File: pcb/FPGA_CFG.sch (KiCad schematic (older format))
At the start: 5 parts, among them U4 iCE40-HX8K-CT256, U6 SERIAL_FLASH

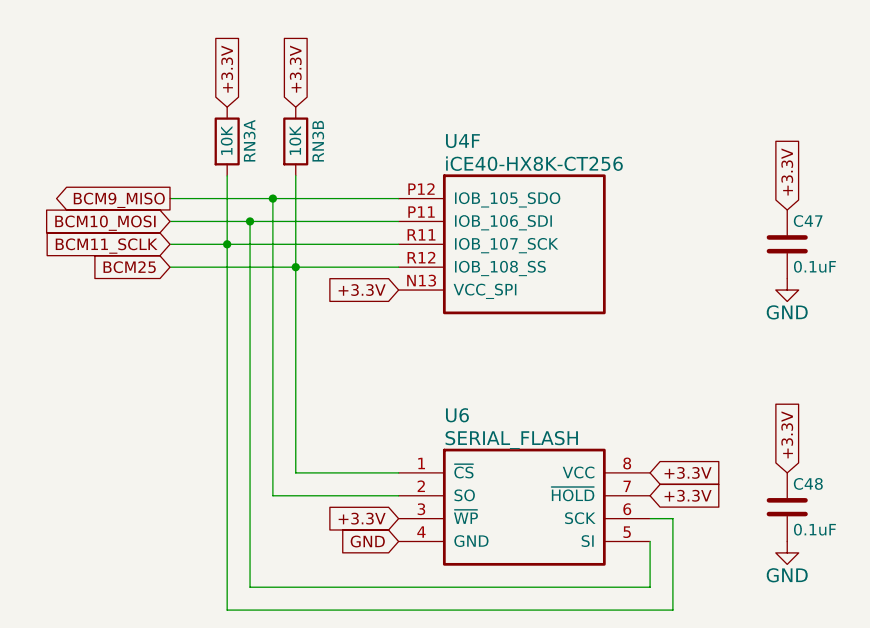
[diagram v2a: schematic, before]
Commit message: Added manufacturer part numbers to the schematic.
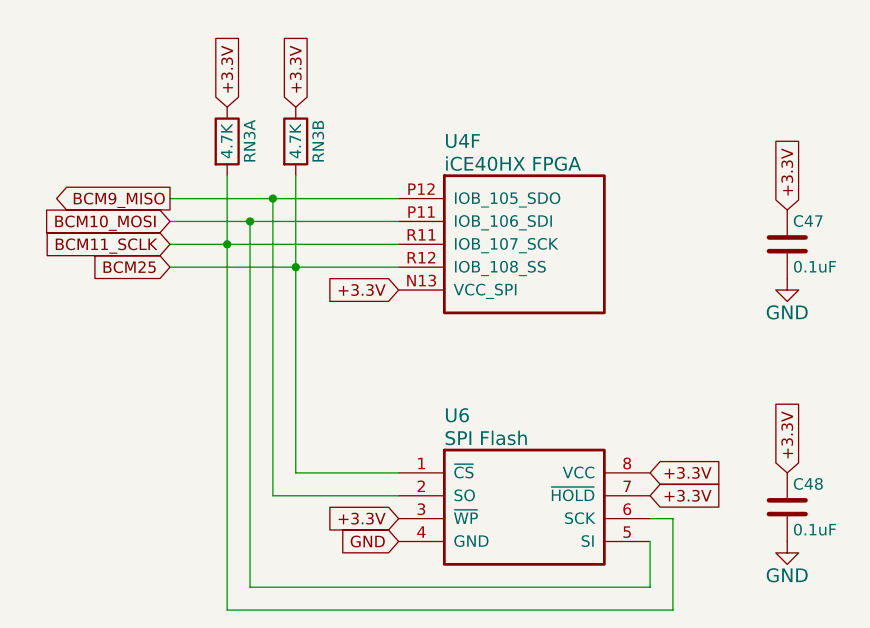
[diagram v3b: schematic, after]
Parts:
- C47, C48: manf# 08055C104KAT2A -> (none)
- RN3: value 10K -> 4.7K
- U4: value iCE40-HX8K-CT256 -> iCE40HX FPGA
- U6: value SERIAL_FLASH -> SPI Flash; manf# (none) -> AT25SF041-SSHD-T
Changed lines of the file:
@@
 AR Path="/55F04F56" Ref="U?"  Part="6"
 F 0 "U4" H 5800 3750 60  0000 L CNN
-F 1 "iCE40-HX8K-CT256" H 5800 3650 60  0000 L CNN
+F 1 "iCE40HX FPGA" H 5800 3650 60  0000 L CNN
 F 2 "XESS:Lattice_caBGA_256" H 5600 3500 60  0001 C CNN
 F 3 "" H 5600 3500 60  0000 C CNN
@@
 P 5600 4700
 F 0 "U6" H 5800 4950 60  0000 L CNN
-F 1 "SERIAL_FLASH" H 5800 4850 60  0000 L CNN
+F 1 "SPI Flash" H 5800 4850 60  0000 L CNN
 F 2 "SMD_Packages:SOIC-8-N" H 5600 4700 50  0001 C CNN
 F 3 "" H 5600 4700 50  0000 C CNN
+F 4 "AT25SF041-SSHD-T" H 5600 4700 60  0001 C CNN "manf#"
 	1    5600 4700
 	1    0    0    -1
@@
 F 2 "Capacitors_SMD:C_0603" H 7338 3550 30  0001 C CNN
 F 3 "" H 7300 3700 60  0000 C CNN
-F 4 "08055C104KAT2A" H 7300 3700 60  0001 C CNN "manf#"
 	1    7300 3700
 	1    0    0    -1
@@
 F 2 "Capacitors_SMD:C_0603" H 7338 4700 30  0001 C CNN
 F 3 "" H 7300 4850 60  0000 C CNN
-F 4 "08055C104KAT2A" H 7300 4850 60  0001 C CNN "manf#"
 	1    7300 4850
 	1    0    0    -1
@@
 P 4850 3400
 F 0 "RN3" H 5000 3300 50  0000 C CNN
-F 1 "10K" H 5000 3400 50  0000 C CNN
+F 1 "4.7K" H 5000 3400 50  0000 C CNN
 F 2 "XESS:CTS_742C043" H 4850 3400 50  0001 C CNN
 F 3 "" H 4850 3400 50  0000 C CNN
@@
 P 5150 3400
 F 0 "RN3" H 5300 3300 50  0000 C CNN
-F 1 "10K" H 5300 3400 50  0000 C CNN
+F 1 "4.7K" H 5300 3400 50  0000 C CNN
 F 2 "XESS:CTS_742C043" H 5150 3400 50  0001 C CNN
 F 3 "" H 5150 3400 50  0000 C CNN
@@
 1E 25 49 2A DA F6 C4 5C B7 0C C3 B9 A4 0A 98 09 FC 0D B0 92 CD 57 CD 1F 06 4E 04 26 A7 75 27 49
 52 39 26 13 73 DE C3 6C BE 70 B5 12 F8 16 86 73 8D C3 FF 03 63 F8 EE 2E BE 9A 04 B1 00 00 00 00
-49 45 4E 44 AE 42 60 82 40
+49 45 4E 44 AE 42 60 82 13
 EndData
 $EndBitmap

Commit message: Fixed some manufacturer's part# assignments.
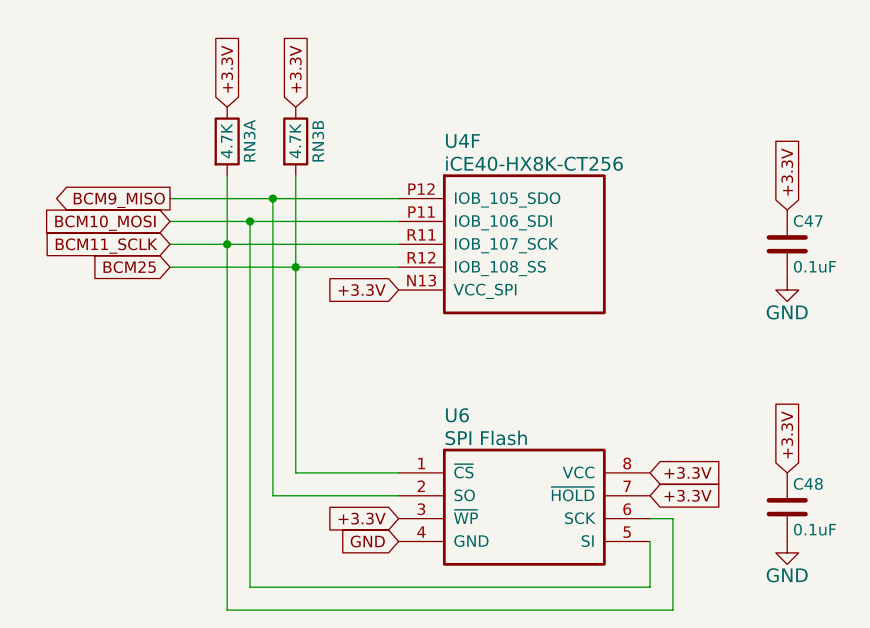
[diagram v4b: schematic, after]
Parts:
- U4: value iCE40HX FPGA -> iCE40-HX8K-CT256
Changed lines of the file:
@@
 AR Path="/55F04F56" Ref="U?"  Part="6"
 F 0 "U4" H 5800 3750 60  0000 L CNN
-F 1 "iCE40HX FPGA" H 5800 3650 60  0000 L CNN
+F 1 "iCE40-HX8K-CT256" H 5800 3650 60  0000 L CNN
 F 2 "XESS:Lattice_caBGA_256" H 5600 3500 60  0001 C CNN
 F 3 "" H 5600 3500 60  0000 C CNN
@@
 04 31 C8 D0 41 0A 41 13 04 41 10 04 41 0C 26 52 3A 80 EA BE 9E 05 41 10 04 41 10 04 D1 6B AA D4
 00 68 01 18 8D 67 6D E1 08 82 20 08 82 20 88 81 AB 1D C0 96 FF 07 B5 9C 9A 2D 6E D5 FC 2D 00 00
-00 00 49 45 4E 44 AE 42 60 82 00
+00 00 49 45 4E 44 AE 42 60 82 73
 EndData
 $EndBitmap
@@
 1E 25 49 2A DA F6 C4 5C B7 0C C3 B9 A4 0A 98 09 FC 0D B0 92 CD 57 CD 1F 06 4E 04 26 A7 75 27 49
 52 39 26 13 73 DE C3 6C BE 70 B5 12 F8 16 86 73 8D C3 FF 03 63 F8 EE 2E BE 9A 04 B1 00 00 00 00
-49 45 4E 44 AE 42 60 82 13
+49 45 4E 44 AE 42 60 82 C2
 EndData
 $EndBitmap

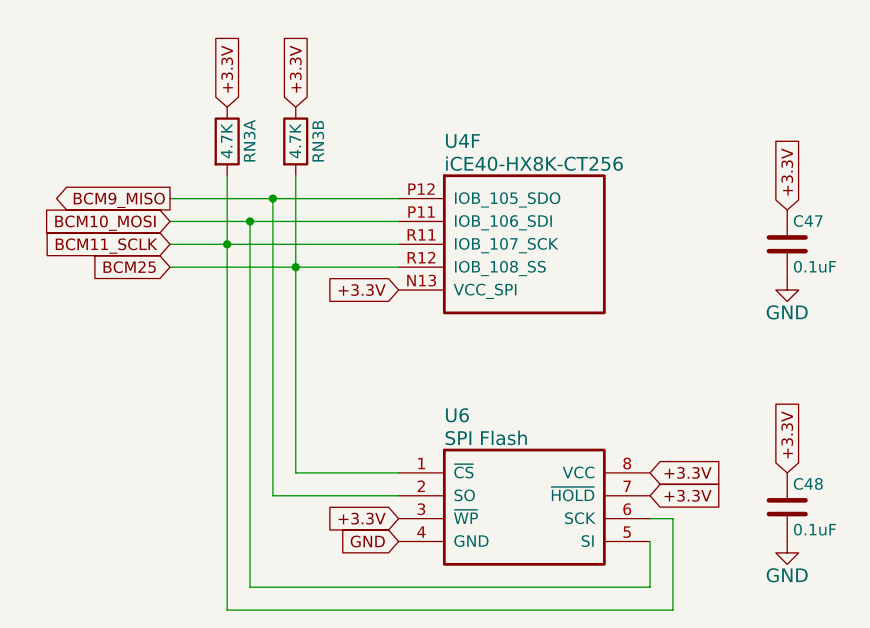
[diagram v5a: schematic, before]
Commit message: Swapped SI and SO connections on SPI flash for FPGA config.
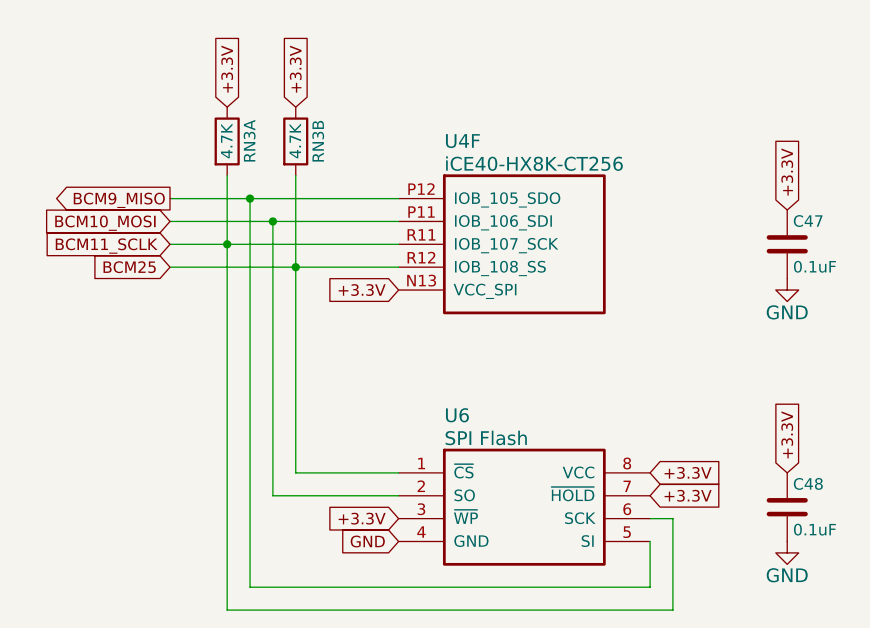
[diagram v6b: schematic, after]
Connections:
- net BCM10_MOSI: now also U6.2 (SO); no longer U6.5 (SI)
- net BCM9_MISO: now also U6.5 (SI); no longer U6.2 (SO)
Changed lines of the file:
@@
 	4600 3500 5600 3500
 Wire Wire Line
-	5050 3500 5050 4800
-Wire Wire Line
 	5050 4800 5600 4800
 Wire Wire Line
@@
 Wire Wire Line
 	6800 4900 6700 4900
-Wire Wire Line
-	4950 3600 4950 5200
 Connection ~ 4850 3700
 Wire Wire Line
@@
 	5150 4700 5600 4700
 Connection ~ 5150 3800
-Connection ~ 5050 3500
-Connection ~ 4950 3600
 Text GLabel 4600 3700 0    50   Input ~ 0
 BCM11_SCLK
@@
 55 BA E9 1E 45 C1 A5 AE 83 10 42 08 21 84 10 62 29 92 A4 84 10 42 08 21 84 10 C2 A9 94 F3 E7 B9
 8E 61 2D AC 28 7C D0 75 10 42 08 21 84 10 42 2C 45 FF 1F 5C 99 D7 EB 78 7F 83 BD 00 00 00 00 49
-45 4E 44 AE 42 60 82 00
+45 4E 44 AE 42 60 82 1B
 EndData
 $EndBitmap
@@
 1E 25 49 2A DA F6 C4 5C B7 0C C3 B9 A4 0A 98 09 FC 0D B0 92 CD 57 CD 1F 06 4E 04 26 A7 75 27 49
 52 39 26 13 73 DE C3 6C BE 70 B5 12 F8 16 86 73 8D C3 FF 03 63 F8 EE 2E BE 9A 04 B1 00 00 00 00
-49 45 4E 44 AE 42 60 82 45
+49 45 4E 44 AE 42 60 82 EF
 EndData
 $EndBitmap
+Wire Wire Line
+	4950 5200 4950 3500
+Connection ~ 4950 3500
+Wire Wire Line
+	5050 4800 5050 3600
+Connection ~ 5050 3600
 $EndSCHEMATC
